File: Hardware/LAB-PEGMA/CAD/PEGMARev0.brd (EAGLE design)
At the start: 203.2 x 203.2 mm, 508 parts, among them J12 MINI-USB-UX60A-MB-5ST, J21 D-SUB9-H2M09RA, J41 FTSH-105-02-F-D, J7 Molex 22-28-4030, K1 G6KU-2P-Y, K2 G6KU-2F-Y, K3 G6K-2P, K4 G6K-2G, Q1 2N2222, Q3 2N2222, Q4 2N2222, Q5 2N2222, SW1 B3SN-3012P, SW2 B3SN-3012P, SW3 B3SN-3012P, U1 STM32F205VG, U10 MAX4376, U11 MCP601R, U12 Molex 500873-0816, U13 MAX4376, U14 MAX4376, U15 LM2623, U16 MCP601R, U17 MCP601R, U18 MAX4376, U19 MAX4376, U2 MCP601R, U20 MAX4376, U21 TPS62240DDC, U22 LM2623, U23 MCP601R, U24 MAX4376, U25 MCP601R, U26 MAX4376, U27 MAX4376, U28 LM2623, U29 MCP601R, U3 TPS62240DDC, U30 MAX4376, U31 MAX4376, U32 LM2623, U33 MCP601R, U34 MAX4376, U35 MAX4376, U36 MAX4376, U37 MAX4376, U38 LM2623, U39 MCP601R, U4 MAX4376, U40 LM2623, U41 MAX4376, U42 LM2623, U43 TPS62240DDC, U44 MCP601R, U45 MCP601R, U46 MAX4376, U47 TPS62240DDC, U48 MCP601R, U49 MAX4376, U5 TPS62240DDC, U50 MCP601R, U51 TPS62240DDC, U52 MCP601R, U53 MAX4376, U54 TPS62240DDC, U55 MAX4376, U56 MAX4376, U57 LM2623, U58 HIH6130, U59 25AA512, U6 MCP601R, U60 25AA512, U61 IS61WV51216-10ZSXI, U62 74HC4067, U63 74HC4067, U64 74HC4067, U65 MAX6520, U66 74HC259, U67 MCP601R, U68 ADM3491ARZ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

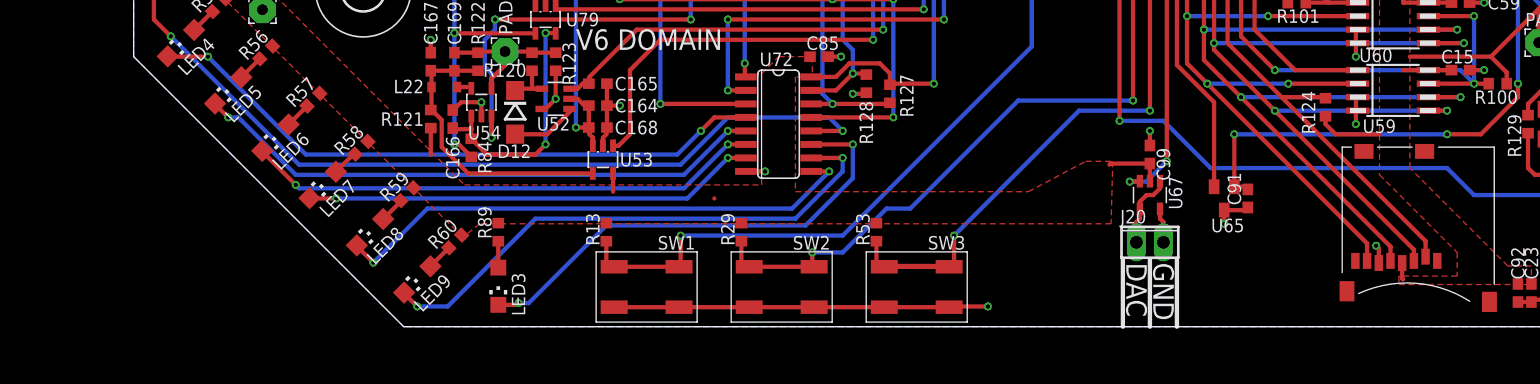
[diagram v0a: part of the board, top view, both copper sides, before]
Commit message: Serial Flash Symbol
Changed the PEGMA board + schematic to reflect the actual serial flash
module populated on it. The board is still rats nested.
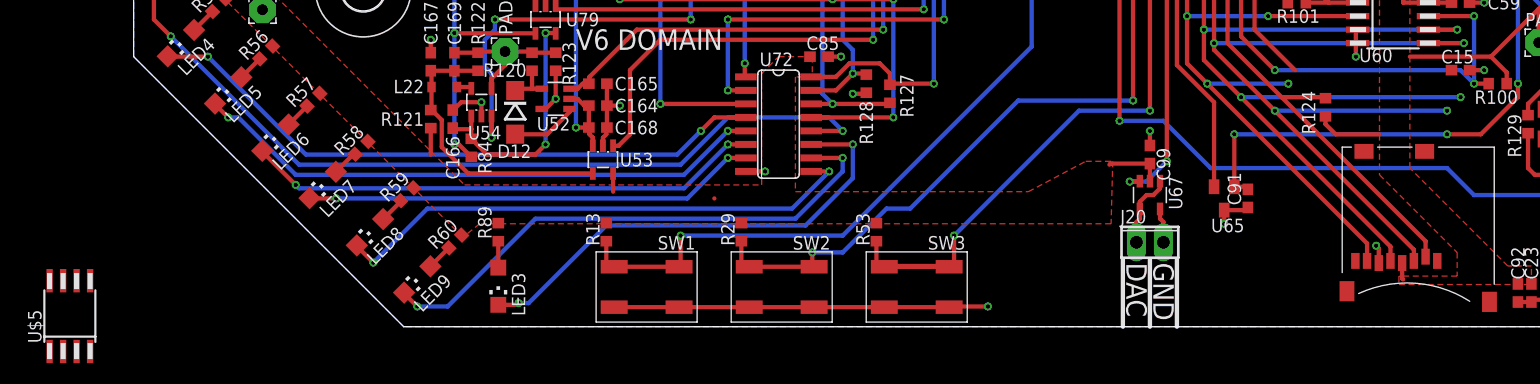
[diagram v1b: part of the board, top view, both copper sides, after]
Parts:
- removed U59: 25AA512, IKE:SO-08M
- added U$5: 25MPX, PEGMA:SO-08M
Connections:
- new net HOLD: U$5.7
- new net SF0CS: U$5.1
- net EE1CS: no longer U59.1
- net EEHLD: no longer U59.7
- net MCUSCK: now also U$5.6; no longer U59.6
- net MCUSDI: now also U$5.2; no longer U59.2
- net MCUSDO: now also U$5.5; no longer U59.5
- net PE: now also U$5.3, U$5.4; no longer U59.3, U59.4
- net V3: now also U$5.8; no longer U59.8
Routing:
- net MCUSDI: track 218.0 -> 211.5 mm
- net EE1CS: track 145.7 -> 139.8 mm
- net V3: track 201.5 -> 197.0 mm
- net EEHLD: track 134.0 -> 129.7 mm
- net MCUSCK: track 218.6 -> 215.6 mm
- net PE: track 636.7 -> 634.0 mm, vias 170 -> 169
- net MCUSDO: track 200.9 -> 199.1 mm

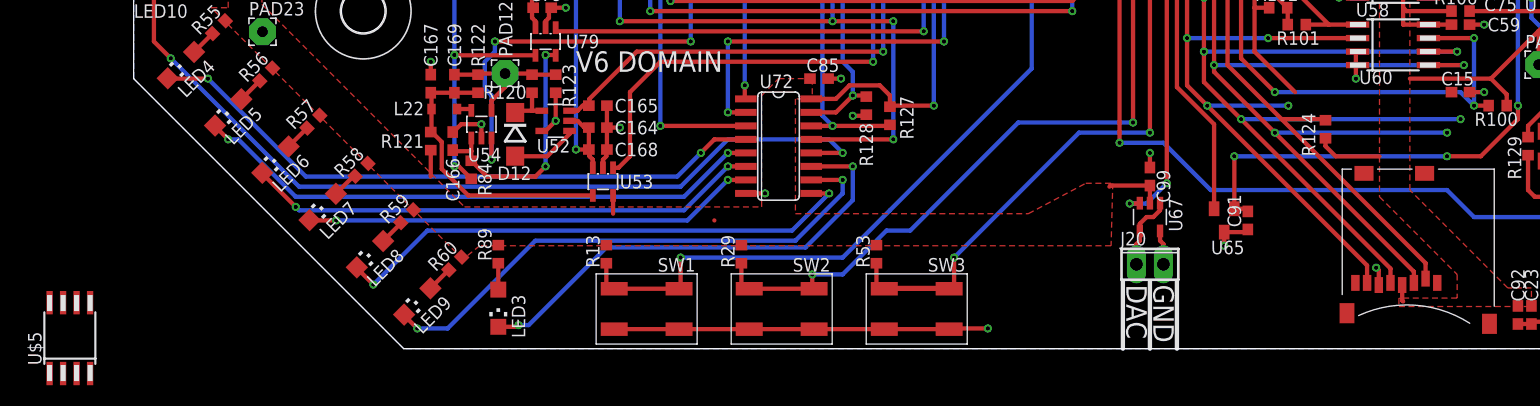
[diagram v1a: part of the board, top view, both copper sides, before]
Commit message: 1) Fixing some inconsistencies that were introduced by changing from an EEPROM symbol to a serial flash symbol
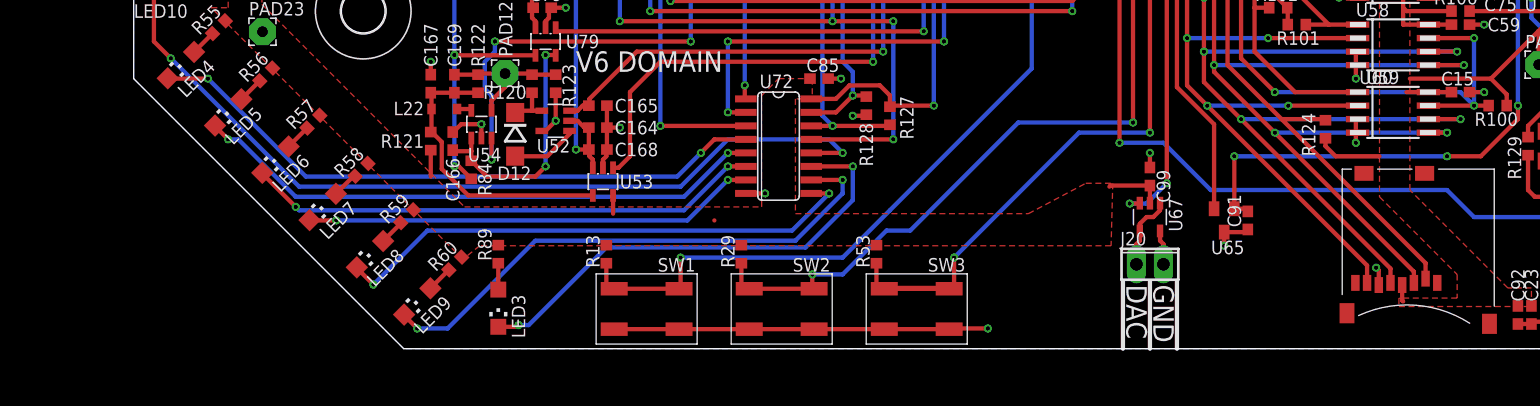
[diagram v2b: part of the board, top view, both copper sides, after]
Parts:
- removed U$5: 25MPX, PEGMA:SO-08M
- added U59: 25MPX, PEGMA:SO-08M
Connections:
- removed net EE1CS: R102.2, U1.95
- removed net HOLD: U$5.7
- net EEHLD: now also U59.7
- net MCUSCK: now also U59.6; no longer U$5.6
- net MCUSDI: now also U59.2; no longer U$5.2
- net MCUSDO: now also U59.5; no longer U$5.5
- net PE: now also U59.3, U59.4; no longer U$5.3, U$5.4
- net SF0CS: now also R102.2, U1.95, U59.1; no longer U$5.1
- net V3: now also U59.8; no longer U$5.8
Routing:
- net SF0CS: track 0.00 -> 145.7 mm, vias 0 -> 4
- net EE1CS: track 139.8 -> 0.00 mm, vias 4 -> 0
- net MCUSDI: track 211.5 -> 218.0 mm
- net EEHLD: track 129.7 -> 134.0 mm
- net V3: track 197.0 -> 201.2 mm
- net MCUSCK: track 215.6 -> 218.6 mm
- net PE: track 634.0 -> 636.5 mm, vias 169 -> 170
- net MCUSDO: track 199.1 -> 200.9 mm
